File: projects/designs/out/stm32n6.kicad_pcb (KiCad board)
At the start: 2 copper layers, 12.2 x 6.7 mm, 112 parts, among them SW1 0R

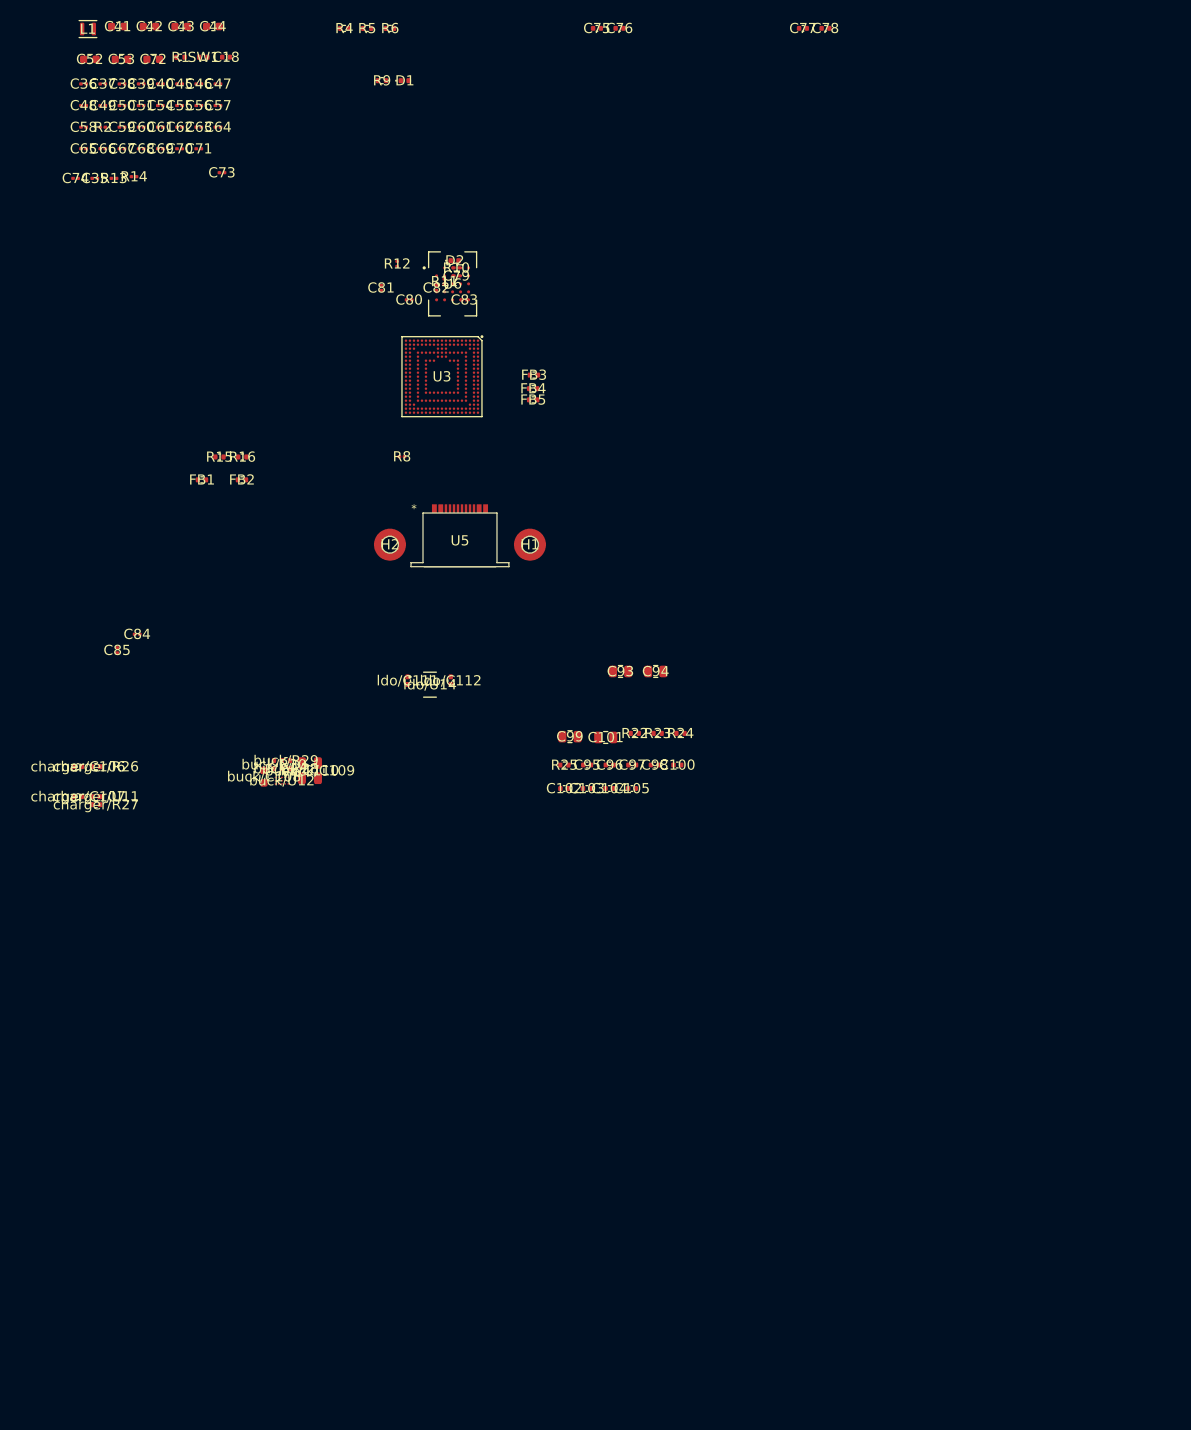
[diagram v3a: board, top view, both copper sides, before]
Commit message: Update stm32n6, blocks, BOMs, and snapshot history
- stm32n6 schematic, layout, BOM, and PCB export refreshed.
- Tweaks to buck-boost, charger, and ldo blocks.
- Regenerate power-6v BOM; add adc-test BOM.
- New stm32n6 history snapshots.

Co-Authored-By: Claude Opus 4.7 (1M context) <noreply@anthropic.com>
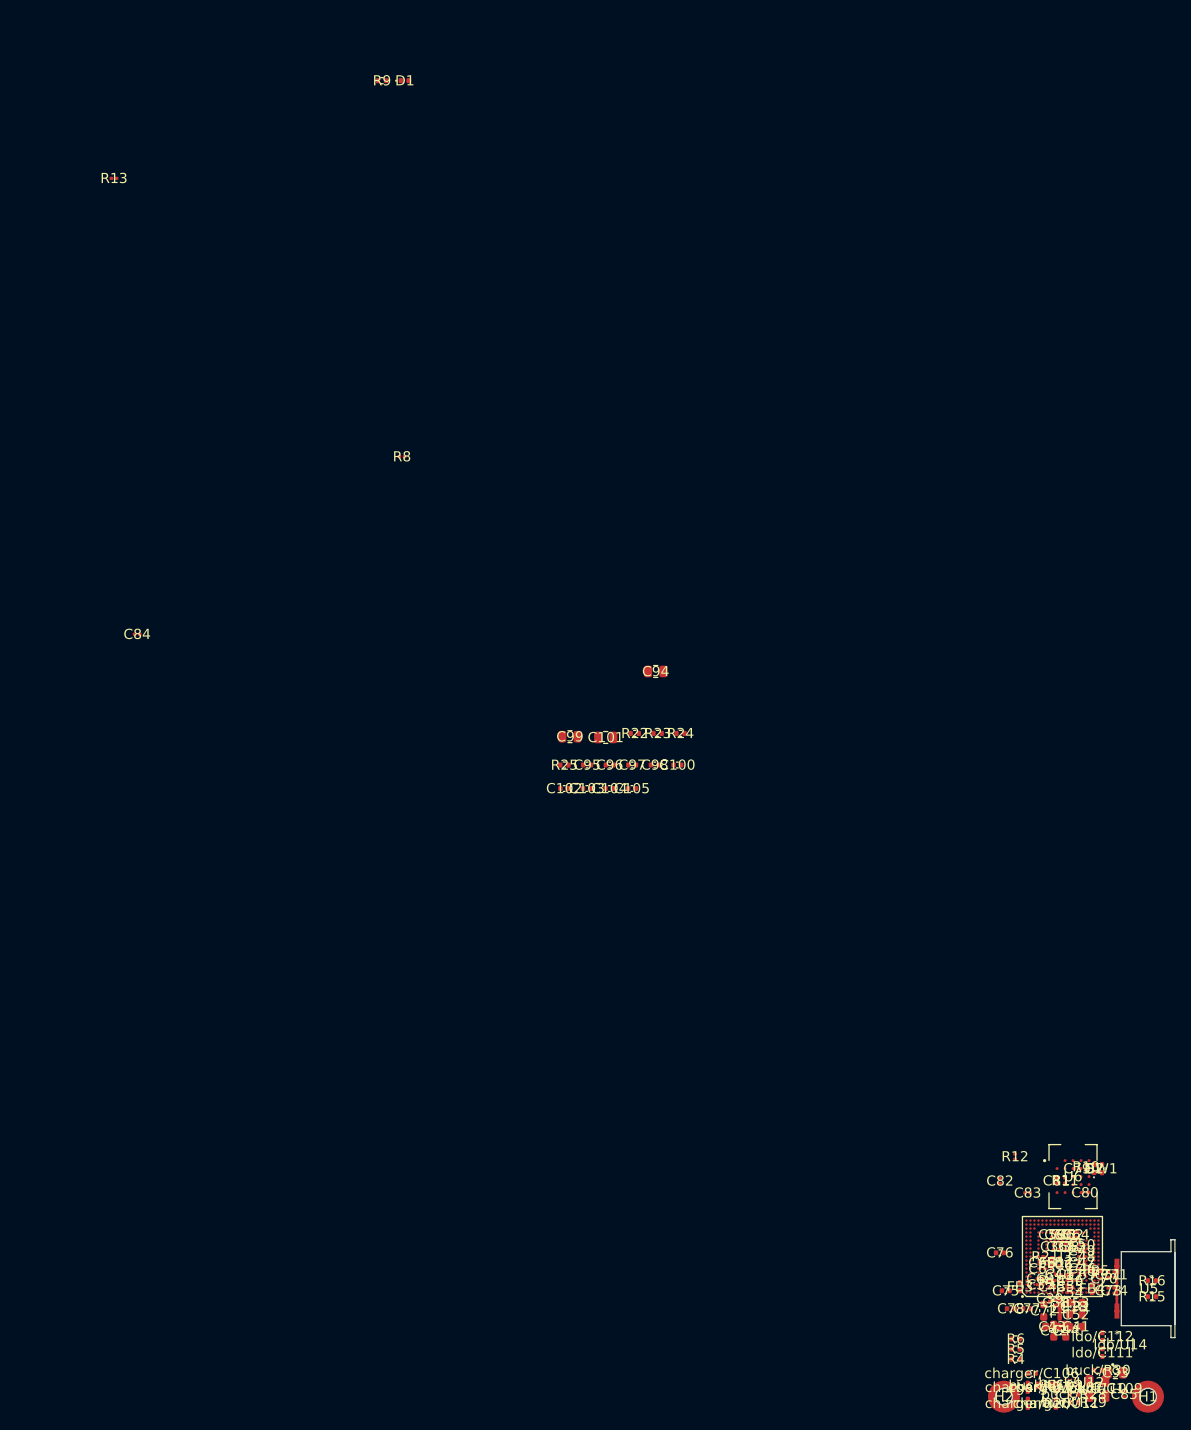
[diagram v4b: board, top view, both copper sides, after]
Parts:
- moved C41 201.9 mm to (148.2, 175.2)
- moved L1 200.8 mm to (146.2, 173.0), turned to -90 degrees
- moved C52 199.5 mm to (148.2, 173.8)
- moved C42 198.4 mm to (145.5, 175.8), turned to -90 degrees
- moved C53 195.9 mm to (148.2, 172.2)
- moved C43 195.6 mm to (145.2, 175.2), turned to 180 degrees
- moved C44 194.8 mm to (147.0, 175.8), turned to -90 degrees
- moved R1 192.6 mm to (149.0, 172.8), turned to 90 degrees
- moved C72 192.0 mm to (144.2, 173.2), turned to -90 degrees
- moved C58 190.7 mm to (145.7, 172.2), turned to -90 degrees
- moved C48 190.5 mm to (149.0, 166.5)
- moved C74 190.2 mm to (153.0, 170.8), turned to -90 degrees
- moved C51 189.7 mm to (152.3, 168.8), turned to -90 degrees
- moved C39 189.6 mm to (145.0, 171.8), turned to -90 degrees
- moved C36 189.3 mm to (145.5, 165.2), turned to -90 degrees
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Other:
- board size 12.2 x 6.7 mm -> 6.7 x 12.2 mm
